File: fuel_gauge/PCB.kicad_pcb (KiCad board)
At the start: 2 copper layers, 100 x 70 mm, 31 parts, among them P1 Con3,123*, P3 Con3,*234, Q1 BSS84, Q2 BSS138, Q3 2N7002, SW1 SPST, SW2 SPST, U1 bq34z100pw

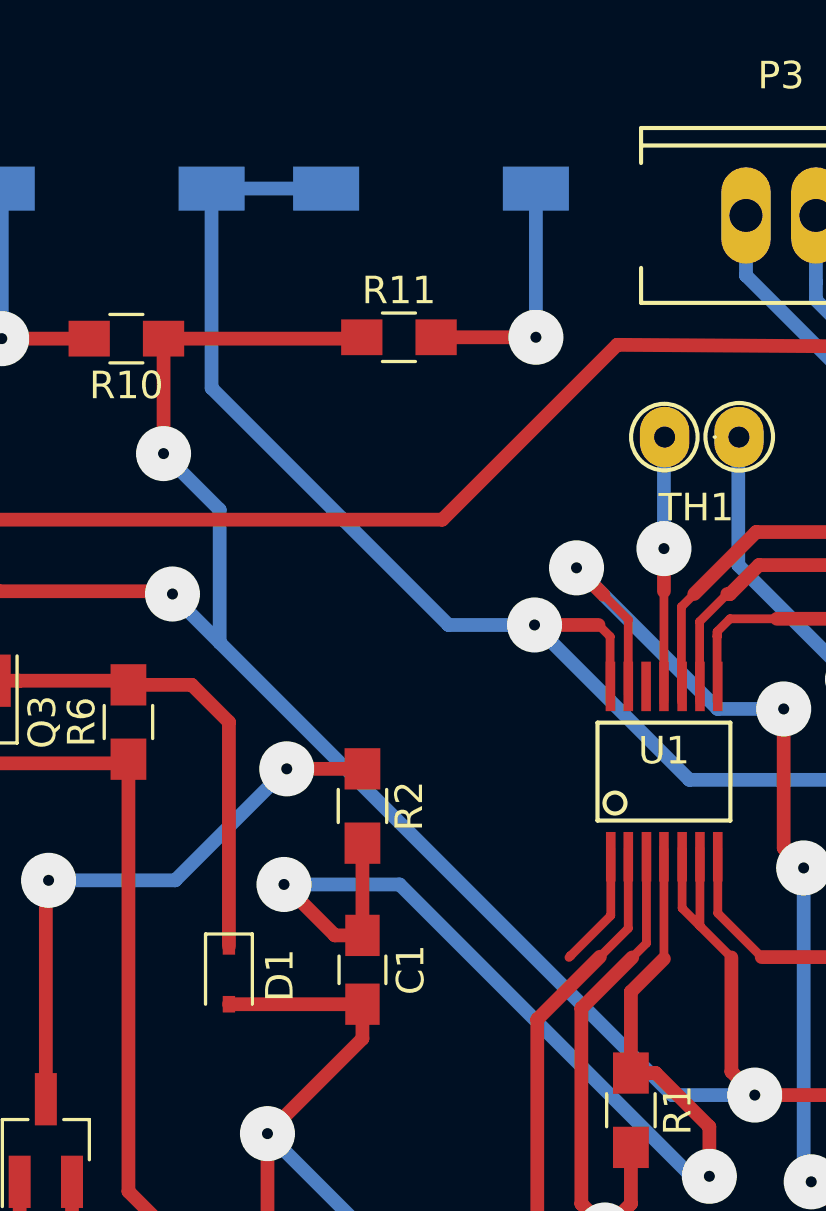
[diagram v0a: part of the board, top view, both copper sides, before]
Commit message: Add library into a separated folder named component-library
Add switches to select PC or Arduino communications
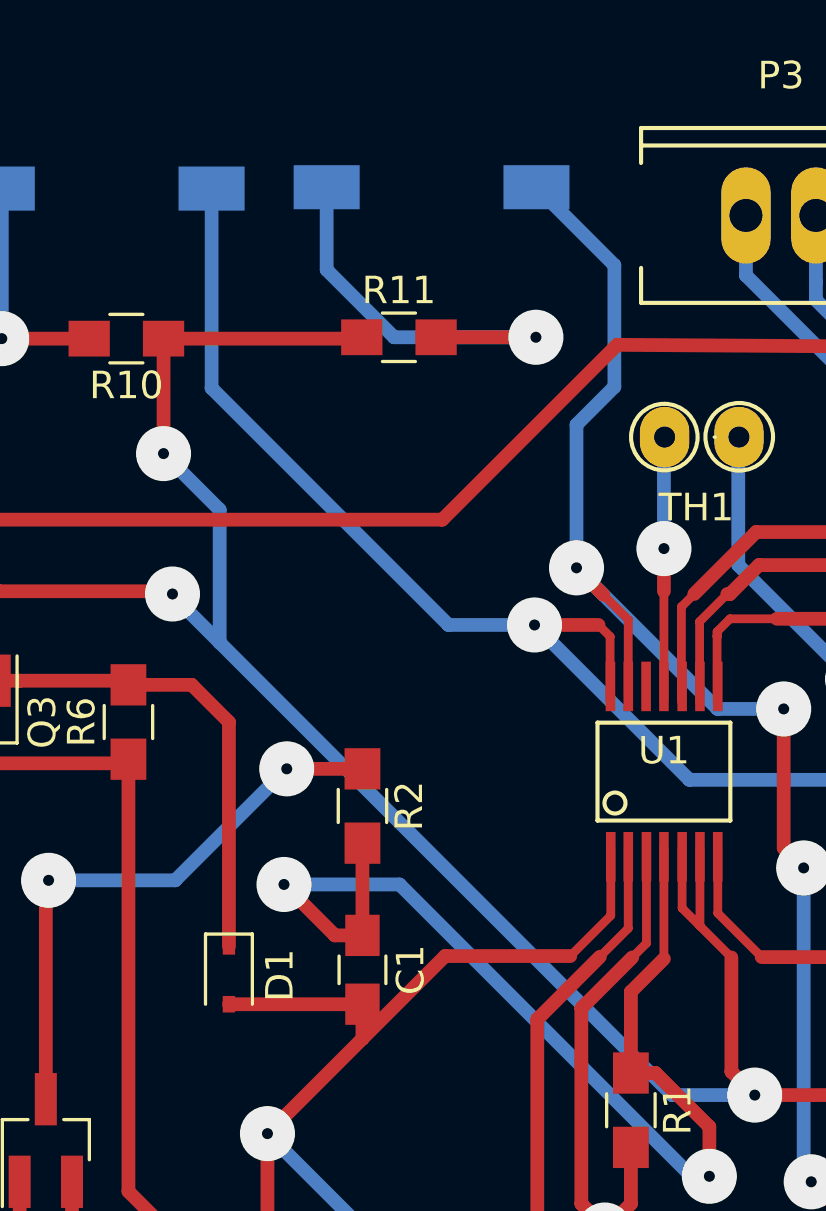
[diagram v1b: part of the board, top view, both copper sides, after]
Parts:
- moved SW2 7.60 mm to (133.5, 75.0), turned to 0 degrees
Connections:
- SW2 pad 2: Net-(R12-Pad2) -> Net-(R13-Pad2)
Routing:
- net Net-(R13-Pad2): track 45.9 -> 61.4 mm
- net GNDREF: track 212.4 -> 221.2 mm
- net Net-(R11-Pad2): track 9.02 -> 15.2 mm
- net Net-(R12-Pad2): track 55.2 -> 51.1 mm
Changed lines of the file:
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@@
   (general
     (links 57)
-    (no_connects 1)
+    (no_connects 0)
     (area 99.949999 59.949999 200.050001 130.050001)
     (thickness 1.6)
     (drawings 18)
-    (tracks 276)
+    (tracks 283)
     (zones 0)
     (modules 31)
@@
     (47 F.CrtYd user hide)
     (48 B.Fab user)
-    (49 F.Fab user)
+    (49 F.Fab user hide)
   )
   (setup
@@
   )
   (module myfootprint:DIP-2_LongPads (layer B.Cu)
-    (at 141.1 75.025 180)
+    (at 133.5 74.975)
     (descr "4-lead dip package, row spacing 7.62 mm (300 mils), LongPads")
     (tags "DIL DIP PDIP 2.54mm 7.62mm 300mil LongPads")
-    (fp_text reference SW2 (at 3.81 2.39 180) (layer B.SilkS)
+    (fp_text reference SW2 (at 3.81 2.39) (layer B.SilkS)
       (effects (font (size 1 1) (thickness 0.15)) (justify mirror))
     )
-    (fp_text value SPST (at 3.81 -3.556 180) (layer B.Fab)
+    (fp_text value SPST (at 3.81 -3.556) (layer B.Fab)
       (effects (font (size 1 1) (thickness 0.15)) (justify mirror))
     )
@@
     (fp_line (start 0.635 1.397) (end 0.635 -1.524) (layer B.Fab) (width 0.15))
     (fp_line (start 6.985 -1.524) (end 0.635 -1.524) (layer B.Fab) (width 0.15))
-    (fp_text user %R (at 4.191 0 180) (layer B.Fab)
+    (fp_text user %R (at 4.191 0) (layer B.Fab)
       (effects (font (size 1 1) (thickness 0.15)) (justify mirror))
     )
-    (pad 1 smd rect (at 0 0 180) (size 2.4 1.6) (layers B.Cu B.Paste B.Mask)
+    (pad 1 smd rect (at 0 0) (size 2.4 1.6) (layers B.Cu B.Paste B.Mask)
       (net 19 "Net-(R11-Pad2)"))
-    (pad 2 smd rect (at 7.62 0 180) (size 2.4 1.6) (layers B.Cu B.Paste B.Mask)
-      (net 21 "Net-(R12-Pad2)"))
+    (pad 2 smd rect (at 7.62 0) (size 2.4 1.6) (layers B.Cu B.Paste B.Mask)
+      (net 22 "Net-(R13-Pad2)"))
     (model ../../../../../../DATOS/UNIVERSIDAD/TFG/PCB/myfootprint.pretty/43613.wrl
       (at (xyz 0.15 0 0))
@@
   (segment (start 134.8 98.8) (end 134.8 102.15) (width 0.5) (layer F.Cu) (net 1) (status 10))
   (segment (start 144.55 107.15) (end 144.55 107.15) (width 0.5) (layer F.Cu) (net 1) (status 30))
+  (segment (start 142.35 102.9) (end 137.8 102.9) (width 0.5) (layer F.Cu) (net 2))
+  (segment (start 137.8 102.9) (end 134.8 105.9) (width 0.5) (layer F.Cu) (net 2))
   (segment (start 171.3 109) (end 175.95 109) (width 0.5) (layer F.Cu) (net 2))
   (segment (start 175.95 109) (end 176.15 108.8) (width 0.5) (layer F.Cu) (net 2))
@@
   (via (at 121.7 80.475) (size 2) (drill 0.4) (layers F.Cu B.Cu) (net 18))
   (segment (start 121.7 80.475) (end 121.7 75.025) (width 0.5) (layer B.Cu) (net 18))
-  (segment (start 137.475 80.425) (end 141.1 80.425) (width 0.5) (layer F.Cu) (net 19))
+  (segment (start 133.5 74.975) (end 133.5 77.975) (width 0.5) (layer B.Cu) (net 19))
   (via (at 141.1 80.425) (size 2) (drill 0.4) (layers F.Cu B.Cu) (net 19))
-  (segment (start 141.1 80.425) (end 141.1 75.025) (width 0.5) (layer B.Cu) (net 19))
+  (segment (start 141.1 80.425) (end 137.475 80.425) (width 0.5) (layer F.Cu) (net 19))
+  (segment (start 135.95 80.425) (end 141.1 80.425) (width 0.5) (layer B.Cu) (net 19))
+  (segment (start 133.5 77.975) (end 135.95 80.425) (width 0.5) (layer B.Cu) (net 19))
   (segment (start 145.75 83.25) (end 145.75 88.1) (width 0.5) (layer B.Cu) (net 20) (status 10))
   (segment (start 145.75 89.65) (end 145.75 88.1) (width 0.5) (layer F.Cu) (net 20))
@@
   (segment (start 129.32 82.27) (end 129.32 75.025) (width 0.5) (layer B.Cu) (net 21))
   (segment (start 137.925 90.875) (end 129.32 82.27) (width 0.5) (layer B.Cu) (net 21))
-  (segment (start 129.32 75.025) (end 133.48 75.025) (width 0.5) (layer B.Cu) (net 21))
   (segment (start 143.7942 91.2942) (end 143.375 90.875) (width 0.32) (layer F.Cu) (net 21))
   (segment (start 143.375 90.875) (end 143.35 90.85) (width 0.32) (layer F.Cu) (net 21))
   (segment (start 143.7942 93.656) (end 143.7942 91.3058) (width 0.32) (layer F.Cu) (net 21))
   (segment (start 143.7942 91.3058) (end 143.7942 91.2942) (width 0.32) (layer F.Cu) (net 21))
+  (segment (start 142.575 88.8) (end 142.575 83.6) (width 0.5) (layer B.Cu) (net 22))
+  (segment (start 143.95 77.805) (end 141.12 74.975) (width 0.5) (layer B.Cu) (net 22))
+  (segment (start 143.95 82.225) (end 143.95 77.805) (width 0.5) (layer B.Cu) (net 22))
+  (segment (start 142.575 83.6) (end 143.95 82.225) (width 0.5) (layer B.Cu) (net 22))
+  (via (at 142.575 88.8) (size 2) (drill 0.4) (layers F.Cu B.Cu) (net 22))
+  (segment (start 142.575 88.8) (end 143.55 89.775) (width 0.5) (layer F.Cu) (net 22))
+  (segment (start 147.7 93.925) (end 142.575 88.8) (width 0.5) (layer B.Cu) (net 22))
+  (segment (start 144.4546 90.6796) (end 143.55 89.775) (width 0.32) (layer F.Cu) (net 22))
+  (segment (start 143.55 89.775) (end 143.525 89.775) (width 0.32) (layer F.Cu) (net 22))
   (segment (start 150.1 93.925) (end 147.7 93.925) (width 0.5) (layer B.Cu) (net 22))
+  (via (at 150.1 93.925) (size 2) (drill 0.4) (layers F.Cu B.Cu) (net 22))
+  (segment (start 150.1 98.975) (end 150.1 93.925) (width 0.5) (layer F.Cu) (net 22))
   (segment (start 156.3 116.3) (end 151.1 111.1) (width 0.5) (layer F.Cu) (net 22))
   (via (at 151.1 111.1) (size 2) (drill 0.4) (layers F.Cu B.Cu) (net 22))
@@
   (via (at 150.825 99.7) (size 2) (drill 0.4) (layers F.Cu B.Cu) (net 22))
   (segment (start 150.825 99.7) (end 150.1 98.975) (width 0.5) (layer F.Cu) (net 22))
-  (segment (start 150.1 98.975) (end 150.1 93.925) (width 0.5) (layer F.Cu) (net 22))
-  (via (at 150.1 93.925) (size 2) (drill 0.4) (layers F.Cu B.Cu) (net 22))
   (segment (start 162.05 116.3) (end 156.3 116.3) (width 0.5) (layer F.Cu) (net 22))
-  (via (at 142.575 88.8) (size 2) (drill 0.4) (layers F.Cu B.Cu) (net 22))
-  (segment (start 142.575 88.8) (end 143.55 89.775) (width 0.5) (layer F.Cu) (net 22))
-  (segment (start 147.7 93.925) (end 142.575 88.8) (width 0.5) (layer B.Cu) (net 22))
   (segment (start 144.4546 93.406) (end 144.4546 90.6796) (width 0.32) (layer F.Cu) (net 22))
-  (segment (start 144.4546 90.6796) (end 143.55 89.775) (width 0.32) (layer F.Cu) (net 22))
-  (segment (start 143.55 89.775) (end 143.525 89.775) (width 0.32) (layer F.Cu) (net 22))
   (segment (start 162.05 116.3) (end 162.05 116.4) (width 0.5) (layer F.Cu) (net 22) (status 30))
 )
